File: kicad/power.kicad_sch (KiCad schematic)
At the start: 60 parts, among them J8 USB_C_Receptacle_PowerOnly_6P, SW1 PH_IND, T1 475uH, U16 TPS2116DRL, U17 PTN5150AHXMP, U22 SN6505BDBV, U23 TPS7A39, U24 TPS62172DSG, U25 TPS62171DSG, U26 TPS7A2009, U27 TPS61391, U28 TPS7A4101

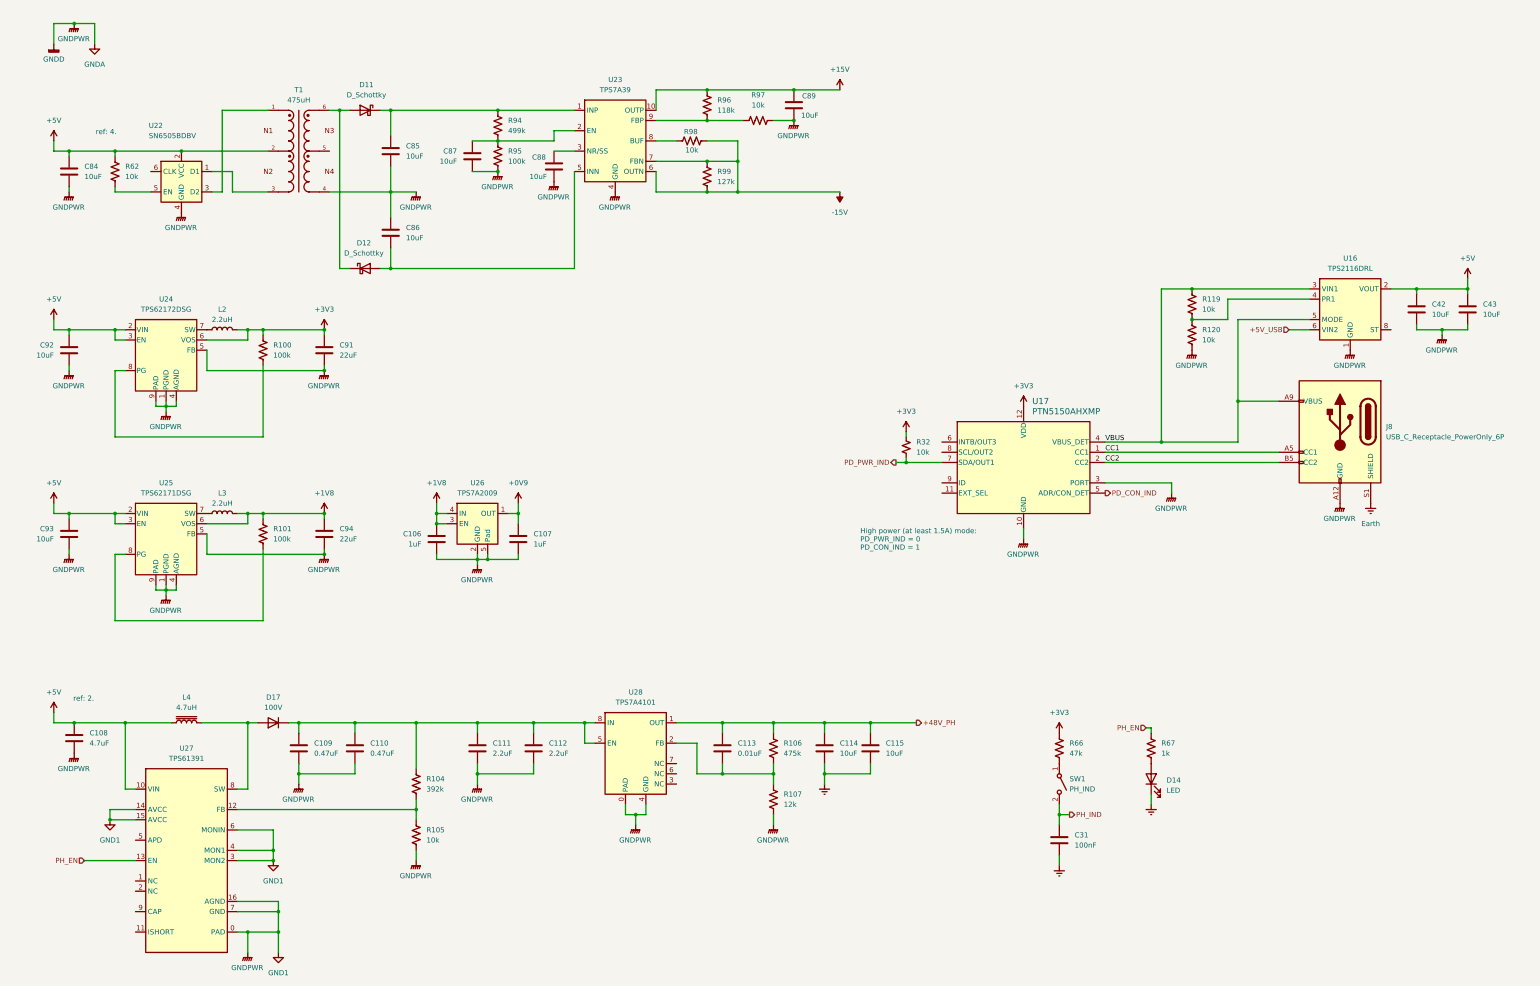
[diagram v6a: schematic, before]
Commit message: CH224K external supply
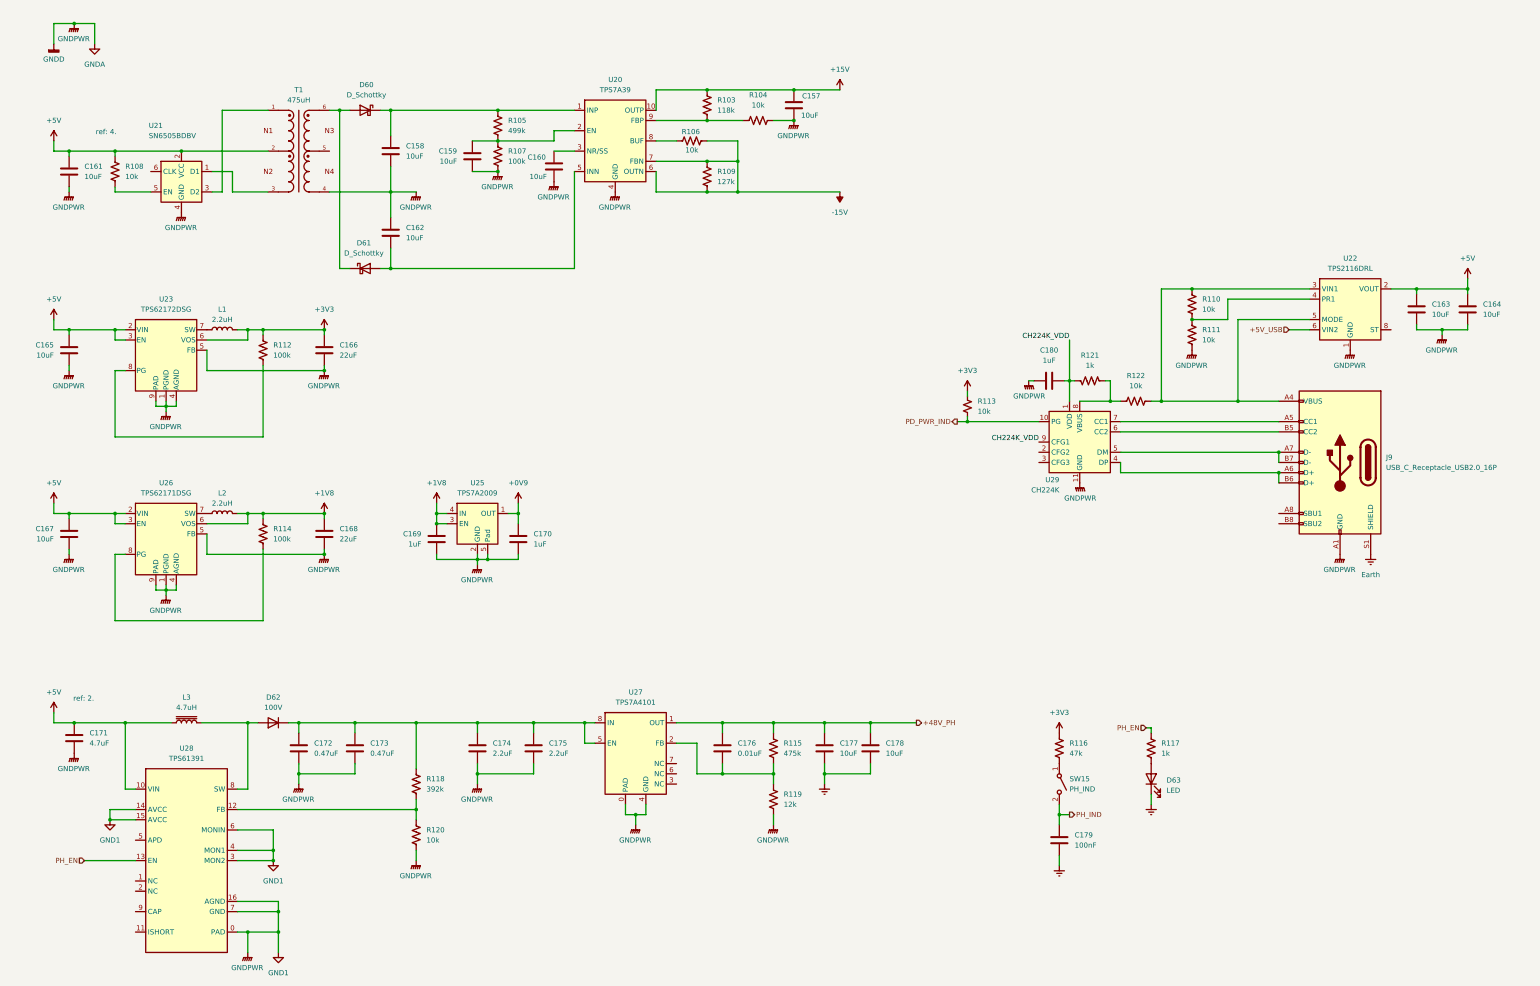
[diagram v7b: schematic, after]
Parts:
- removed J8: USB_C_Receptacle_PowerOnly_6P, symbol Connector:USB_C_Receptacle_PowerOnly_6P
- removed U17: PTN5150AHXMP, SOT1355-1_X2QFN12_NXP, symbol openmic:PTN5150AHXMP
- added C180: 1uF, symbol Device:C
- added J9: USB_C_Receptacle_USB2.0_16P, symbol Connector:USB_C_Receptacle_USB2.0_16P
- added R121: 1k, symbol Device:R_US
- added R122: 10k, symbol Device:R_US
- added U29: CH224K, Package_SO:SSOP-10-1EP_3.9x4.9mm_P1mm_EP2.1x3.3mm, symbol Interface_USB:CH224K
- renumbered C89 to C157, C85 to C158, C87 to C159, C88 to C160, C84 to C161, C86 to C162, C42 to C163, C43 to C164, C92 to C165, C91 to C166, C93 to C167, C94 to C168, C106 to C169, C107 to C170, C108 to C171, C109 to C172, C110 to C173, C111 to C174, C112 to C175, C113 to C176, C114 to C177, C115 to C178, C31 to C179, D11 to D60, D12 to D61, D17 to D62, D14 to D63, L2 to L1, L3 to L2, L4 to L3, R96 to R103, R97 to R104, R94 to R105, R98 to R106, R95 to R107, R62 to R108, R99 to R109, R119 to R110, R120 to R111, R100 to R112, R32 to R113, R101 to R114, R106 to R115, R66 to R116, R67 to R117, R104 to R118, R107 to R119, R105 to R120, SW1 to SW15, U23 to U20, U22 to U21, U16 to U22, U24 to U23, U26 to U25, U25 to U26, U28 to U27, U27 to U28
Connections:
- net Earth: now also J9.S1 (SHIELD)
- net GND1: now also C180.2, J9.A1 (GND), J9.A12 (GND), J9.B1 (GND), J9.B12 (GND), U29.11 (GND)
- net PD_PWR_IND: now also U29.10 (PG)
- net VBUS: no longer names the net of R110.1, U22.3 (VIN1), U22.5 (MODE)
- net VBUS: now also J9.A4 (VBUS), J9.A9 (VBUS), J9.B4 (VBUS), J9.B9 (VBUS), R122.2
- new net: R121.1, R122.1, U29.8 (VBUS)
- new net: J9.A5 (CC1), U29.7 (CC1)
- new net: J9.A6 (D+), J9.B6 (D+), U29.4 (DP)
- new net: J9.A7 (D-), J9.B7 (D-), U29.5 (DM)
- new net: J9.B5 (CC2), U29.6 (CC2)
- new net CH224K_VDD: C180.1, R121.2, U29.1 (VDD), U29.9 (CFG1)
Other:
- note removed: "High power (at least 1.5A) mode: PD_PWR_IND = 0 PD_CON_IND = 1"
- moved on the sheet: R113

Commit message: bypass caps
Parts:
- added C197: 100nF, symbol Device:C_Small
- added C198: 10uF, symbol Device:C_Small
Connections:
- net GND1: now also C197.2, C198.1
- net VBUS: now reaches J9.A4 (VBUS), J9.A9 (VBUS), J9.B4 (VBUS), J9.B9 (VBUS), R110.1, R122.2, U22.3 (VIN1), U22.5 (MODE)
- net VBUS: now also C197.1, C198.2
- net CC1: now reaches J9.A5 (CC1), U29.7 (CC1)
- net DP: now reaches J9.A6 (D+), J9.B6 (D+), U29.4 (DP)
- net DM: now reaches J9.A7 (D-), J9.B7 (D-), U29.5 (DM)
- net CC2: now reaches J9.B5 (CC2), U29.6 (CC2)
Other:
- moved on the sheet: C180, R113, R121, R122, U29
